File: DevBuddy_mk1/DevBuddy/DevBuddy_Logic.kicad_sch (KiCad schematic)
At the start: 38 parts, among them J1 2171820001, J3 Debug Conn, U1 RP2354B, U15 NCP1117-3.3_SOT223, Y1 12MHz

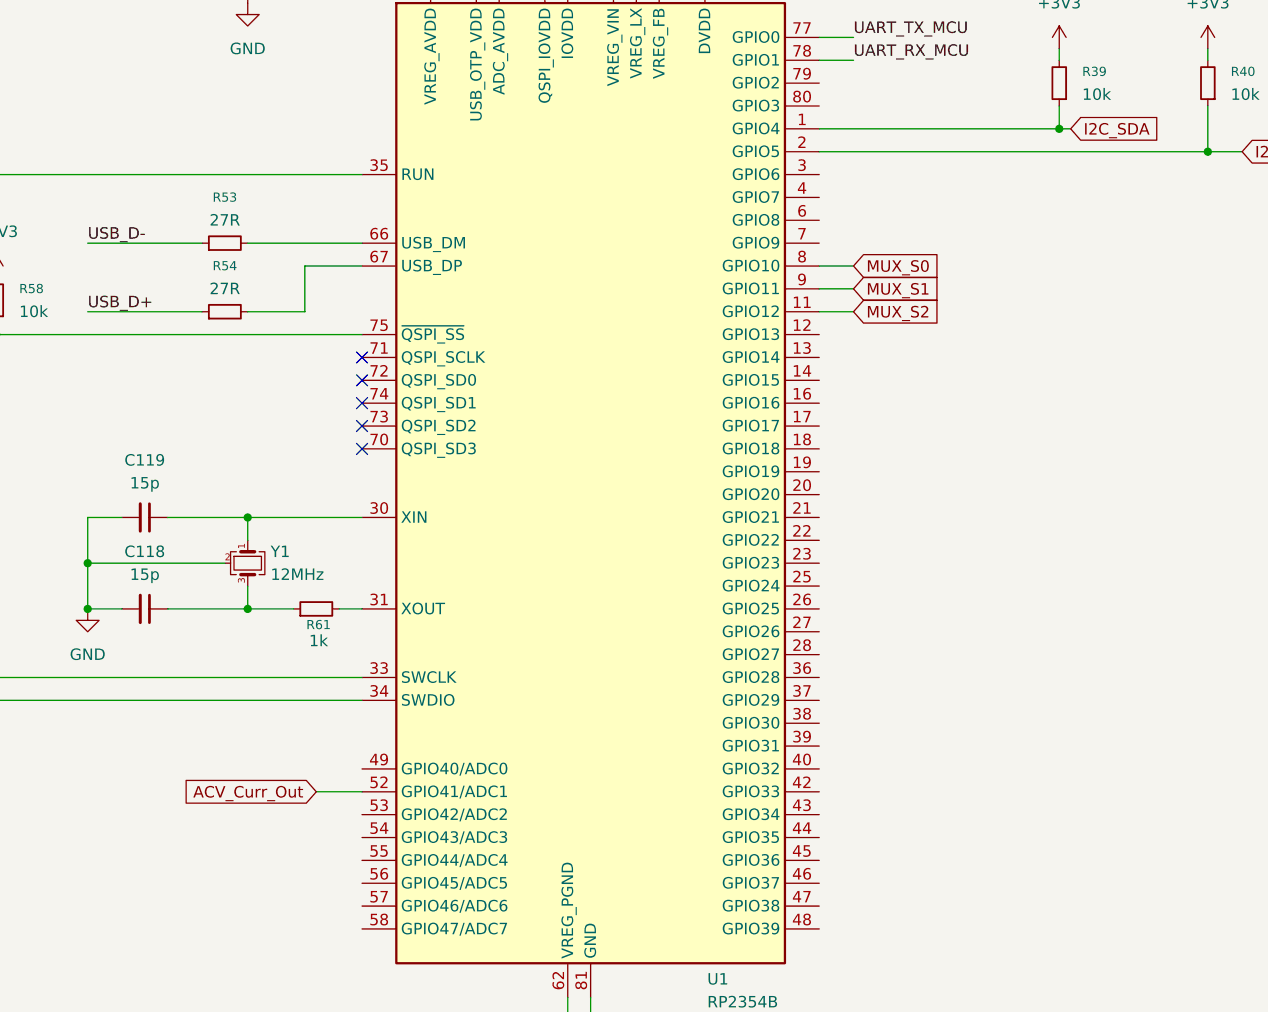
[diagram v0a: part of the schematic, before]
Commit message: More work into the PCB, mainly connectors
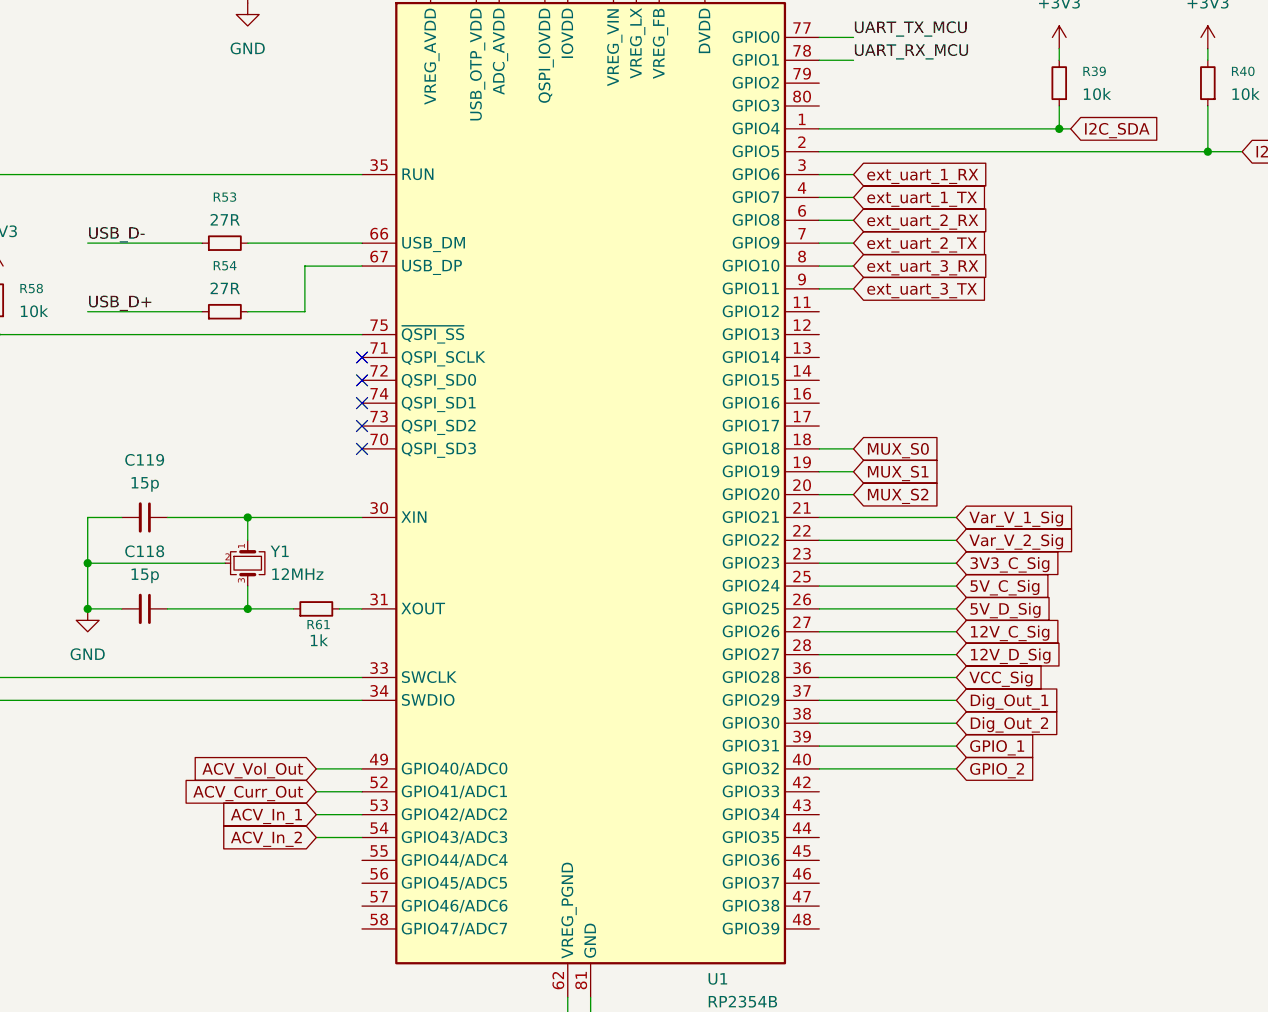
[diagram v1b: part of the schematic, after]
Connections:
- net MUX_S0: now also U1.18 (GPIO18); no longer U1.8 (GPIO10)
- net MUX_S1: now also U1.19 (GPIO19); no longer U1.9 (GPIO11)
- net MUX_S2: now also U1.20 (GPIO20); no longer U1.11 (GPIO12)
- net Var_V_1_Sig: now reaches U1.21 (GPIO21)
- net Var_V_2_Sig: now reaches U1.22 (GPIO22)
- net 3V3_C_Sig: now reaches U1.23 (GPIO23)
- net 5V_C_Sig: now reaches U1.25 (GPIO24)
- net 5V_D_Sig: now reaches U1.26 (GPIO25)
- net 12V_C_Sig: now reaches U1.27 (GPIO26)
- net 12V_D_Sig: now reaches U1.28 (GPIO27)
- net ext_uart_1_RX: now reaches U1.3 (GPIO6)
- net VCC_Sig: now reaches U1.36 (GPIO28)
- net Dig_Out_1: now reaches U1.37 (GPIO29)
- net Dig_Out_2: now reaches U1.38 (GPIO30)
- net GPIO_1: now reaches U1.39 (GPIO31)
- net ext_uart_1_TX: now reaches U1.4 (GPIO7)
- net GPIO_2: now reaches U1.40 (GPIO32)
- net ACV_Vol_Out: now reaches U1.49 (GPIO40/ADC0)
- net ACV_In_1: now reaches U1.53 (GPIO42/ADC2)
- net ACV_In_2: now reaches U1.54 (GPIO43/ADC3)
- net ext_uart_2_RX: now reaches U1.6 (GPIO8)
- net ext_uart_2_TX: now reaches U1.7 (GPIO9)
- new net ext_uart_3_RX: U1.8 (GPIO10)
- new net ext_uart_3_TX: U1.9 (GPIO11)

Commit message: PCB, Progress in routing.
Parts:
- removed J1: 2171820001, USB-C_Vertical:CONN_2171820001_MOL, symbol USB-C_Vertical:2171820001
- removed R55, R56: 5k1, Resistor_SMD:R_0402_1005Metric, symbol Device:R_Small
- added C133, C134: 100n, Capacitor_SMD:C_0402_1005Metric, symbol Device:C_Small
- added J1: 10118194-0001LF, usb_micro_b:AMPHENOL_10118194-0001LF, symbol 10118194-0001LF:10118194-0001LF
- J3: footprint Connector_PinHeader_2.54mm:PinHeader_1x05_P2.54mm_Vertical -> Connector_PinHeader_2.54mm:PinHeader_1x05_P2.54mm_Vertical_SMD_Pin1Left
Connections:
- net +3V3: now also C133.1, C134.1
- net +VBus: now also J1.1 (VCC)
- net GND: now also C133.2, C134.2, J1.5 (GND), J1.SH1 (SHIELD), J1.SH2 (SHIELD), J1.SH3 (SHIELD), J1.SH4 (SHIELD), J1.SH5 (SHIELD), J1.SH6 (SHIELD)
- net USB_D+: now also J1.3 (D+)
- net USB_D-: now also J1.2 (D-)
- net D-: now reaches R53.2, U1.66 (USB_DM)
- net D+: now reaches R54.2, U1.67 (USB_DP)
- no-connect marks 7 -> 6
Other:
- moved on the sheet: C107, C108, C109, C110, C111, C112, C113, C116, C117

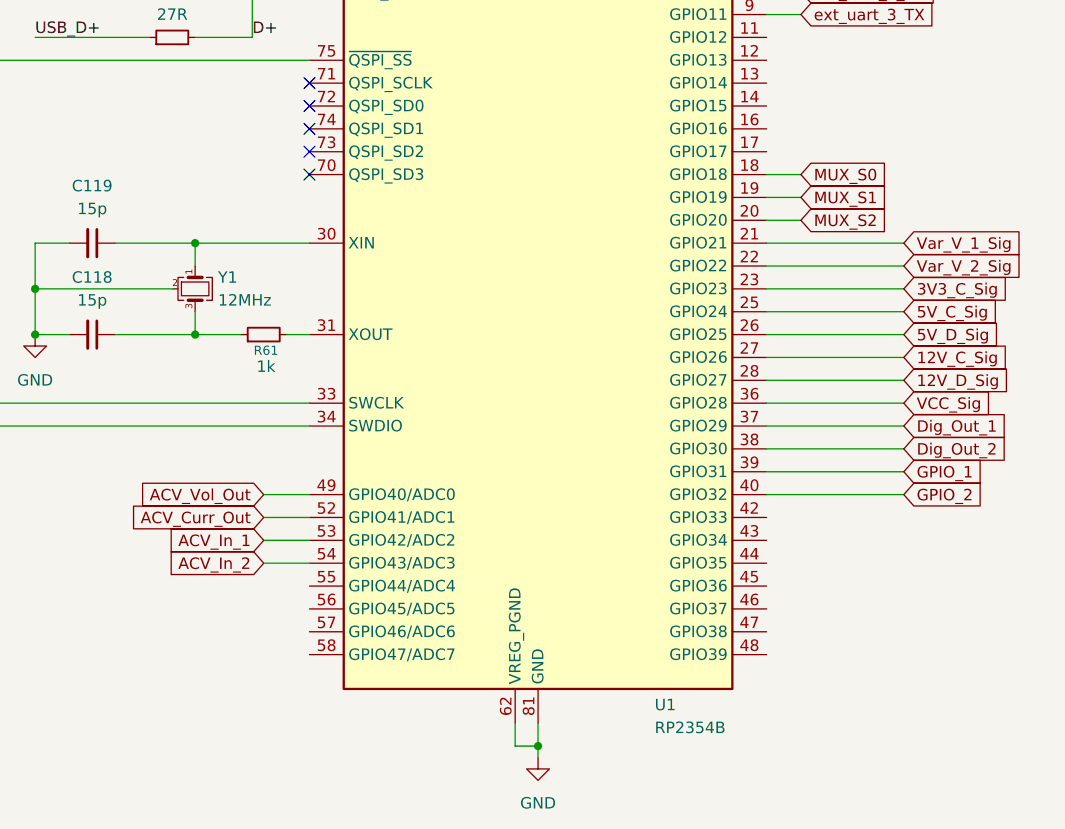
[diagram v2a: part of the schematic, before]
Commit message: PCB, Power routing nearly complete.
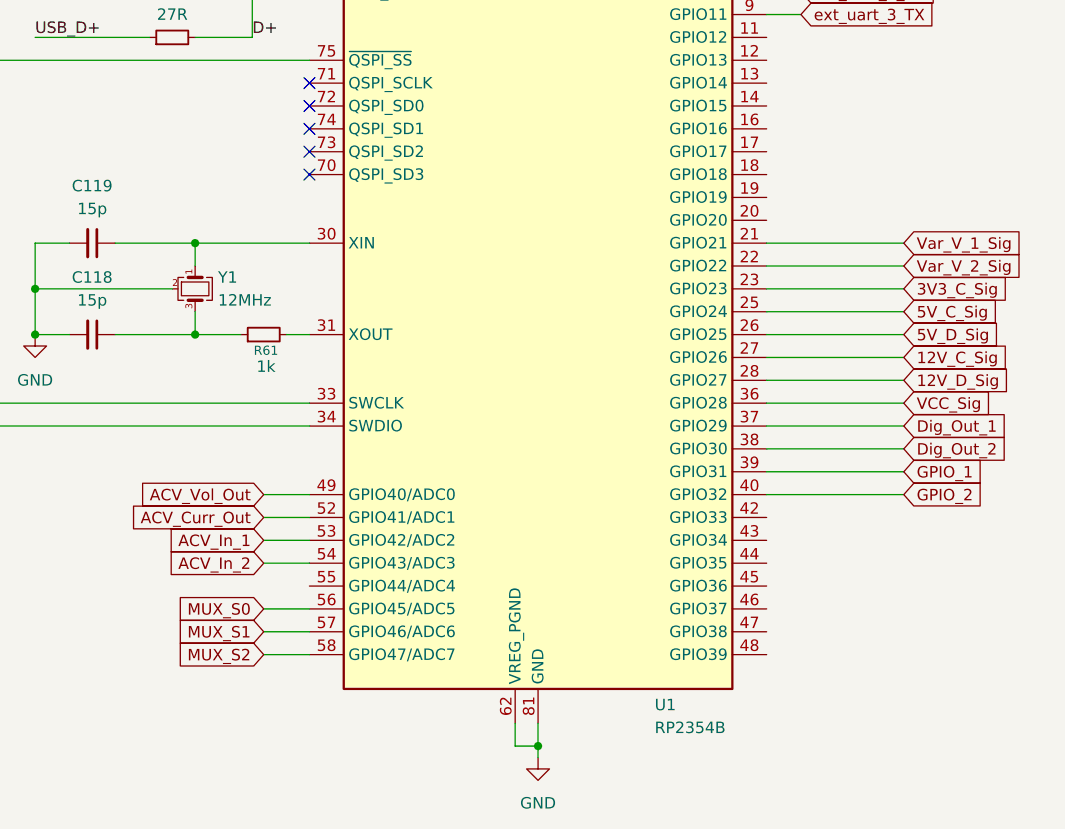
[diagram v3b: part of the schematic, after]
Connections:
- net MUX_S0: now also U1.56 (GPIO45/ADC5); no longer U1.18 (GPIO18)
- net MUX_S1: now also U1.57 (GPIO46/ADC6); no longer U1.19 (GPIO19)
- net MUX_S2: now also U1.58 (GPIO47/ADC7); no longer U1.20 (GPIO20)
